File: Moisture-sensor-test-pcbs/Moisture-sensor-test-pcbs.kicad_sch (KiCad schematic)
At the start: 5 parts

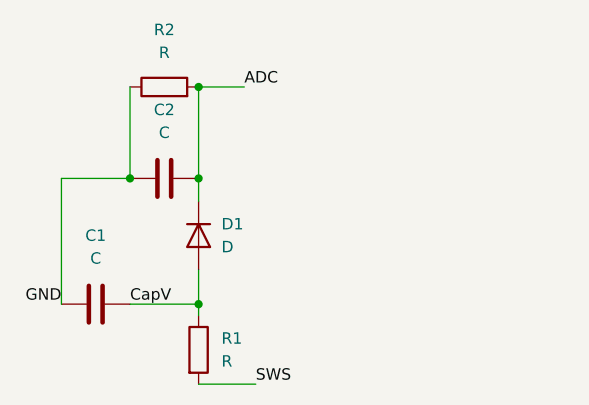
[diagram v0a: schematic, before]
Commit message: Board: Change from 2-layer to 4-layer board
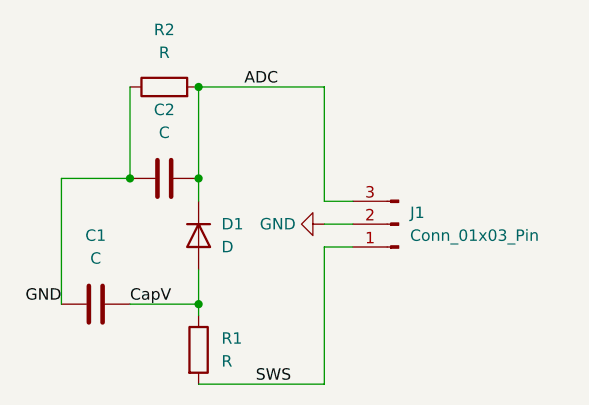
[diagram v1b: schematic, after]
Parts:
- added J1: Conn_01x03_Pin, ThroughHoleParts:PinHeader1x03, symbol Connector:Conn_01x03_Pin
- D1: footprint ThroughHoleParts:Resistor -> ThroughHoleParts:Diode
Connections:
- net ADC: now also J1.3 (Pin_3)
- net GND: now also J1.2 (Pin_2)
- net SWS: now also J1.1 (Pin_1)
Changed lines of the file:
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@@
   (junction (at 125.73 48.26) (diameter 0) (color 0 0 0 0)
   )
-  (wire (pts (xy 125.73 48.26) (xy 130.81 48.26))
+  (wire (pts (xy 125.73 48.26) (xy 139.7 48.26))
     (stroke (width 0) (type default))
   )
@@
     (stroke (width 0) (type default))
   )
-  (wire (pts (xy 125.73 81.28) (xy 132.08 81.28))
+  (wire (pts (xy 125.73 81.28) (xy 139.7 81.28))
     (stroke (width 0) (type default))
   )
@@
     (stroke (width 0) (type default))
   )
+  (wire (pts (xy 139.7 63.5) (xy 142.875 63.5))
+    (stroke (width 0) (type default))
+  )
+  (wire (pts (xy 139.7 48.26) (xy 139.7 60.96))
+    (stroke (width 0) (type default))
+  )
   (wire (pts (xy 118.11 58.42) (xy 110.49 58.42))
     (stroke (width 0) (type default))
   )
+  (wire (pts (xy 139.7 81.28) (xy 139.7 66.04))
+    (stroke (width 0) (type default))
+  )
+  (wire (pts (xy 139.7 66.04) (xy 142.875 66.04))
+    (stroke (width 0) (type default))
+  )
   (wire (pts (xy 125.73 48.26) (xy 125.73 58.42))
     (stroke (width 0) (type default))
   )
   (wire (pts (xy 118.11 72.39) (xy 125.73 72.39))
+    (stroke (width 0) (type default))
+  )
+  (wire (pts (xy 139.7 60.96) (xy 142.875 60.96))
     (stroke (width 0) (type default))
   )
@@
       (effects (font (size 1.27 1.27)) (justify left))
     )
-    (property "Footprint" "ThroughHoleParts:Resistor" (at 125.73 64.77 0)
+    (property "Footprint" "ThroughHoleParts:Diode" (at 125.73 64.77 0)
       (effects (font (size 1.27 1.27)) hide)
     )
@@
         (path "/49ff29a4-b2cd-4d0c-b78e-fc998d4144f9"
           (reference "D1") (unit 1)
+        )
+      )
+    )
+  )
+  (symbol (lib_id "power:GND") (at 139.7 63.5 270) (unit 1)
+    (in_bom yes) (on_board yes) (dnp no) (fields_autoplaced)
+    (property "Reference" "#PWR01" (at 133.35 63.5 0)
+      (effects (font (size 1.27 1.27)) hide)
+    )
+    (property "Value" "GND" (at 136.525 63.5 90)
+      (effects (font (size 1.27 1.27)) (justify right))
+    )
+    (property "Footprint" "" (at 139.7 63.5 0)
+      (effects (font (size 1.27 1.27)) hide)
+    )
+    (property "Datasheet" "" (at 139.7 63.5 0)
+      (effects (font (size 1.27 1.27)) hide)
+    )
+    (pin "1")
+    (instances
+      (project "Moisture-sensor-test-pcbs"
+        (path "/49ff29a4-b2cd-4d0c-b78e-fc998d4144f9"
+          (reference "#PWR01") (unit 1)
         )
       )
@@
         )
       )
+    )
+  )
+  (symbol (lib_id "Connector:Conn_01x03_Pin") (at 147.955 63.5 180) (unit 1)
+    (in_bom yes) (on_board yes) (dnp no) (fields_autoplaced)
+    (property "Reference" "J1" (at 149.225 62.23 0)
+      (effects (font (size 1.27 1.27)) (justify right))
+    )
+    (property "Value" "Conn_01x03_Pin" (at 149.225 64.77 0)
+      (effects (font (size 1.27 1.27)) (justify right))
+    )
+    (property "Footprint" "ThroughHoleParts:PinHeader1x03" (at 147.955 63.5 0)
+      (effects (font (size 1.27 1.27)) hide)
+    )
+    (property "Datasheet" "~" (at 147.955 63.5 0)
+      (effects (font (size 1.27 1.27)) hide)
+    )
+    (pin "3")
+    (pin "1")
+    (pin "2")
+    (instances
+      (project "Moisture-sensor-test-pcbs"
+        (path "/49ff29a4-b2cd-4d0c-b78e-fc998d4144f9"
+          (reference "J1") (unit 1)
+        )
+      )
